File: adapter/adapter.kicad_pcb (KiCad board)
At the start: 2 copper layers, 96 x 18 mm, 26 parts, among them J11 MALE, J12 FEMALE, J13 MALE, J14 STANDOFF, J15 STANDOFF, J16 STANDOFF, J2 FEMALE, J3 STANDOFF, J4 STANDOFF, J5 STANDOFF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

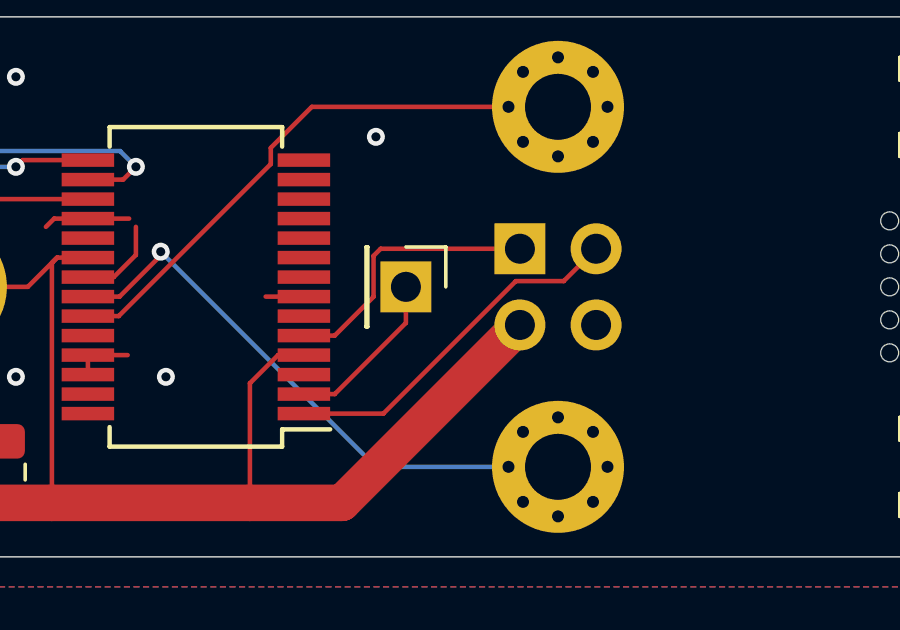
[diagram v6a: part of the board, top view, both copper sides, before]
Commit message: Swap RX/TX on lower board
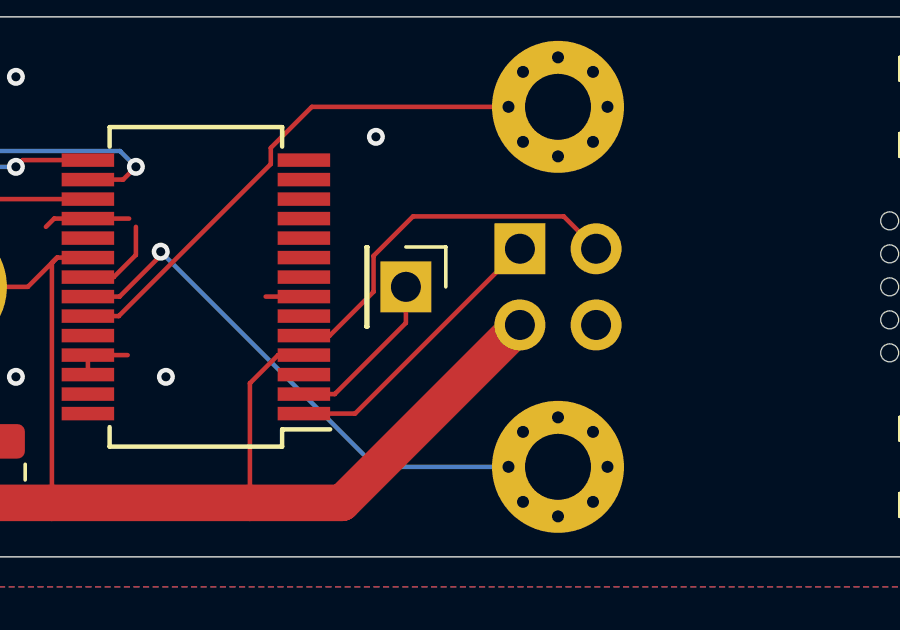
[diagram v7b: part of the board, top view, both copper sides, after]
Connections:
- J2 pad 1: /Lower Board/RXD -> /Lower Board/TXD
- J2 pad 2: /Lower Board/TXD -> /Lower Board/RXD
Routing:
- net /Lower Board/RXD: track 9.20 -> 12.5 mm
- net /Lower Board/TXD: track 12.0 -> 9.48 mm
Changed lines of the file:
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@@
     (thickness 1.6)
     (drawings 392)
-    (tracks 150)
+    (tracks 149)
     (zones 0)
     (modules 26)
@@
     )
     (pad 1 thru_hole rect (at 0 0 180) (size 1.7 1.7) (drill 1) (layers *.Cu *.Mask)
+      (net 10 "/Lower Board/TXD"))
+    (pad 2 thru_hole oval (at -2.54 0 180) (size 1.7 1.7) (drill 1) (layers *.Cu *.Mask)
       (net 9 "/Lower Board/RXD"))
-    (pad 2 thru_hole oval (at -2.54 0 180) (size 1.7 1.7) (drill 1) (layers *.Cu *.Mask)
-      (net 10 "/Lower Board/TXD"))
     (pad 3 thru_hole oval (at 0 -2.54 180) (size 1.7 1.7) (drill 1) (layers *.Cu *.Mask)
       (net 32 +5VB))
@@
   (segment (start 128 111) (end 134.07 111) (width 0.1524) (layer B.Cu) (net 8))
   (segment (start 120.827423 103.827423) (end 128 111) (width 0.1524) (layer B.Cu) (net 8))
-  (segment (start 128.158518 103.73) (end 132.8 103.73) (width 0.1524) (layer F.Cu) (net 9))
-  (segment (start 127.921399 103.967119) (end 128.158518 103.73) (width 0.1524) (layer F.Cu) (net 9))
-  (segment (start 127.921399 105.331001) (end 127.921399 103.967119) (width 0.1524) (layer F.Cu) (net 9))
-  (segment (start 126.6274 106.625) (end 127.921399 105.331001) (width 0.1524) (layer F.Cu) (net 9))
-  (segment (start 125.6 106.625) (end 126.6274 106.625) (width 0.1524) (layer F.Cu) (net 9))
-  (segment (start 134.261399 104.808601) (end 135.34 103.73) (width 0.1524) (layer F.Cu) (net 10))
-  (segment (start 132.665069 104.808601) (end 134.261399 104.808601) (width 0.1524) (layer F.Cu) (net 10))
-  (segment (start 128.24867 109.225) (end 132.665069 104.808601) (width 0.1524) (layer F.Cu) (net 10))
-  (segment (start 125.6 109.225) (end 128.24867 109.225) (width 0.1524) (layer F.Cu) (net 10))
+  (segment (start 129.237119 102.651399) (end 134.261399 102.651399) (width 0.1524) (layer F.Cu) (net 9))
+  (segment (start 127.921399 103.967119) (end 129.237119 102.651399) (width 0.1524) (layer F.Cu) (net 9))
+  (segment (start 127.921399 105.165083) (end 127.921399 103.967119) (width 0.1524) (layer F.Cu) (net 9))
+  (segment (start 134.261399 102.651399) (end 135.34 103.73) (width 0.1524) (layer F.Cu) (net 9))
+  (segment (start 126.461482 106.625) (end 127.921399 105.165083) (width 0.1524) (layer F.Cu) (net 9))
+  (segment (start 125.6 106.625) (end 126.461482 106.625) (width 0.1524) (layer F.Cu) (net 9))
+  (segment (start 127.305 109.225) (end 125.6 109.225) (width 0.1524) (layer F.Cu) (net 10))
+  (segment (start 132.8 103.73) (end 127.305 109.225) (width 0.1524) (layer F.Cu) (net 10))
   (segment (start 107.1276 105.75) (end 107.85 105.75) (width 0.1524) (layer F.Cu) (net 11))
   (segment (start 107.1276 104.75) (end 107.051399 104.826201) (width 0.1524) (layer F.Cu) (net 11))
